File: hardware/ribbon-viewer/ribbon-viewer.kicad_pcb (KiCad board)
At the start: 2 copper layers, 96.5 x 73.7 mm, 186 parts, among them J1 Conn_01x40, J2 Conn_01x40, J3 Power, U1 74HC541, U2 74HC541, U3 74HC541, U4 74HC541, U5 74HC541, U6 MCP1825S

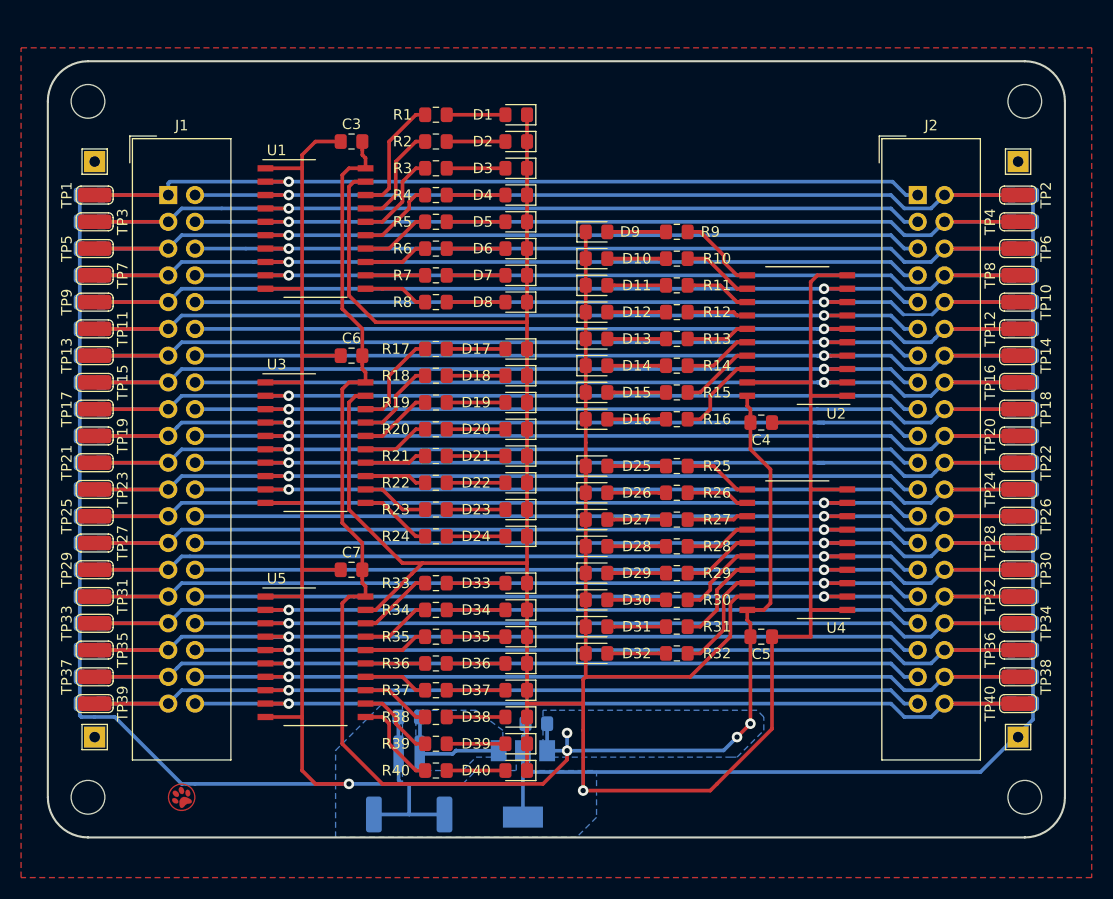
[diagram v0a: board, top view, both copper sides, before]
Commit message: Updated layout
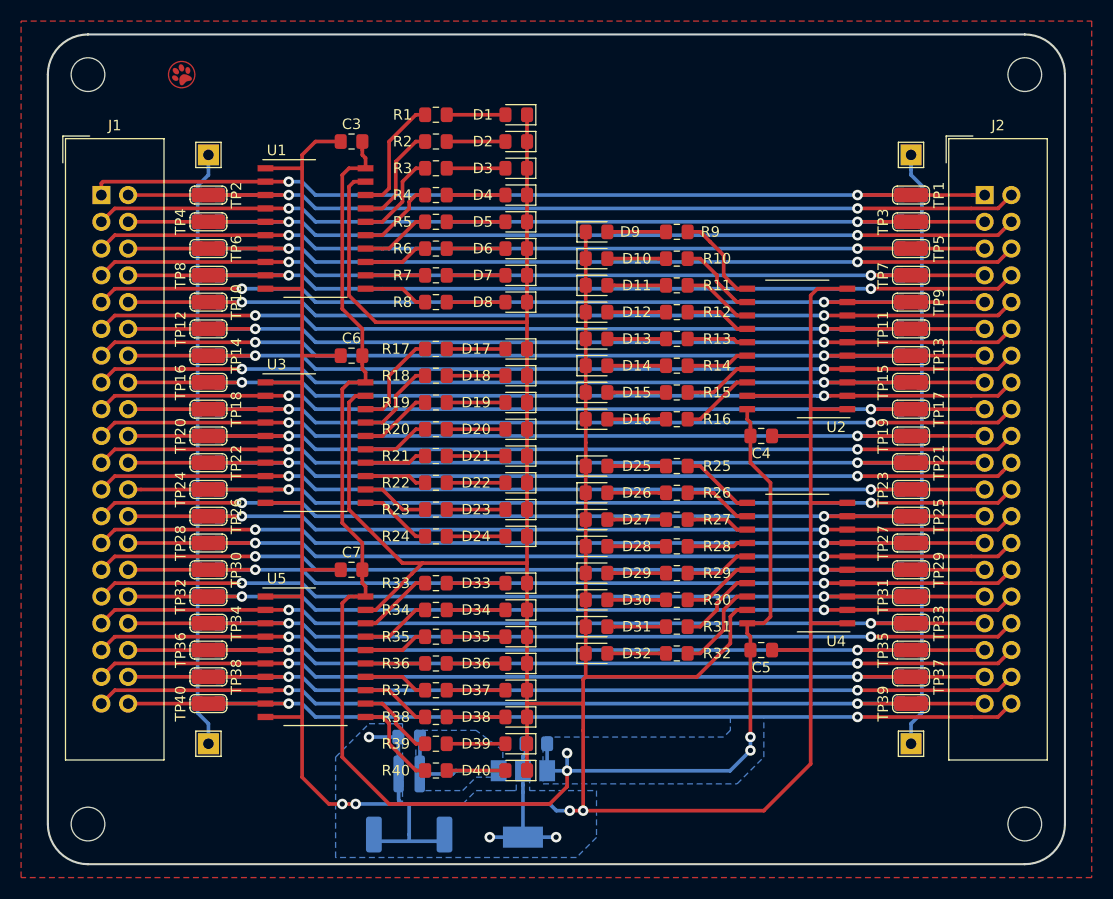
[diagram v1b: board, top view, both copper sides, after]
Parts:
- moved R41 77.9 mm to (134.0, 50.8), turned to 180 degrees
- moved R43 77.9 mm to (134.0, 53.3), turned to 180 degrees
- moved R45 77.9 mm to (134.0, 55.9), turned to 180 degrees
- moved R47 77.9 mm to (134.0, 58.4), turned to 180 degrees
- moved R49 77.9 mm to (134.0, 61.0), turned to 180 degrees
- moved R51 77.9 mm to (134.0, 63.5), turned to 180 degrees
- moved R53 77.9 mm to (134.0, 66.0), turned to 180 degrees
- moved R55 77.9 mm to (134.0, 68.6), turned to 180 degrees
- moved R57 77.9 mm to (134.0, 71.1), turned to 180 degrees
- moved R59 77.9 mm to (134.0, 73.7), turned to 180 degrees
- moved R61 77.9 mm to (134.0, 76.2), turned to 180 degrees
- moved R63 77.9 mm to (134.0, 78.7), turned to 180 degrees
- moved R65 77.9 mm to (134.0, 81.3), turned to 180 degrees
- moved R67 77.9 mm to (134.0, 83.8), turned to 180 degrees
- moved R69 77.9 mm to (134.0, 86.4), turned to 180 degrees
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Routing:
- net GND: track 617.6 -> 575.7 mm, vias 2 -> 7
- net /D38: track 87.7 -> 92.1 mm, vias 1 -> 2
- net /D29: track 87.7 -> 92.1 mm, vias 1 -> 2
- net /D27: track 87.7 -> 92.1 mm, vias 1 -> 2
- net /D25: track 87.7 -> 92.1 mm, vias 1 -> 2
- net /D15: track 87.7 -> 92.1 mm, vias 1 -> 2
- net /D9: track 87.7 -> 92.1 mm, vias 1 -> 2
- net /D31: track 87.7 -> 92.1 mm, vias 1 -> 2
- net /D11: track 87.7 -> 92.1 mm, vias 1 -> 2
- net /D8: track 87.7 -> 91.5 mm, vias 1 -> 2
- net /D6: track 87.7 -> 91.5 mm, vias 1 -> 2
- net /D40: track 87.7 -> 91.5 mm, vias 1 -> 2
- net /D4: track 87.7 -> 91.5 mm, vias 1 -> 2
- net /D36: track 87.7 -> 91.5 mm, vias 1 -> 2
- net /D34: track 87.7 -> 91.5 mm, vias 1 -> 2
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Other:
- board size 96.5 x 73.7 mm -> 96.5 x 78.7 mm

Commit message: Change testpoints to pin header
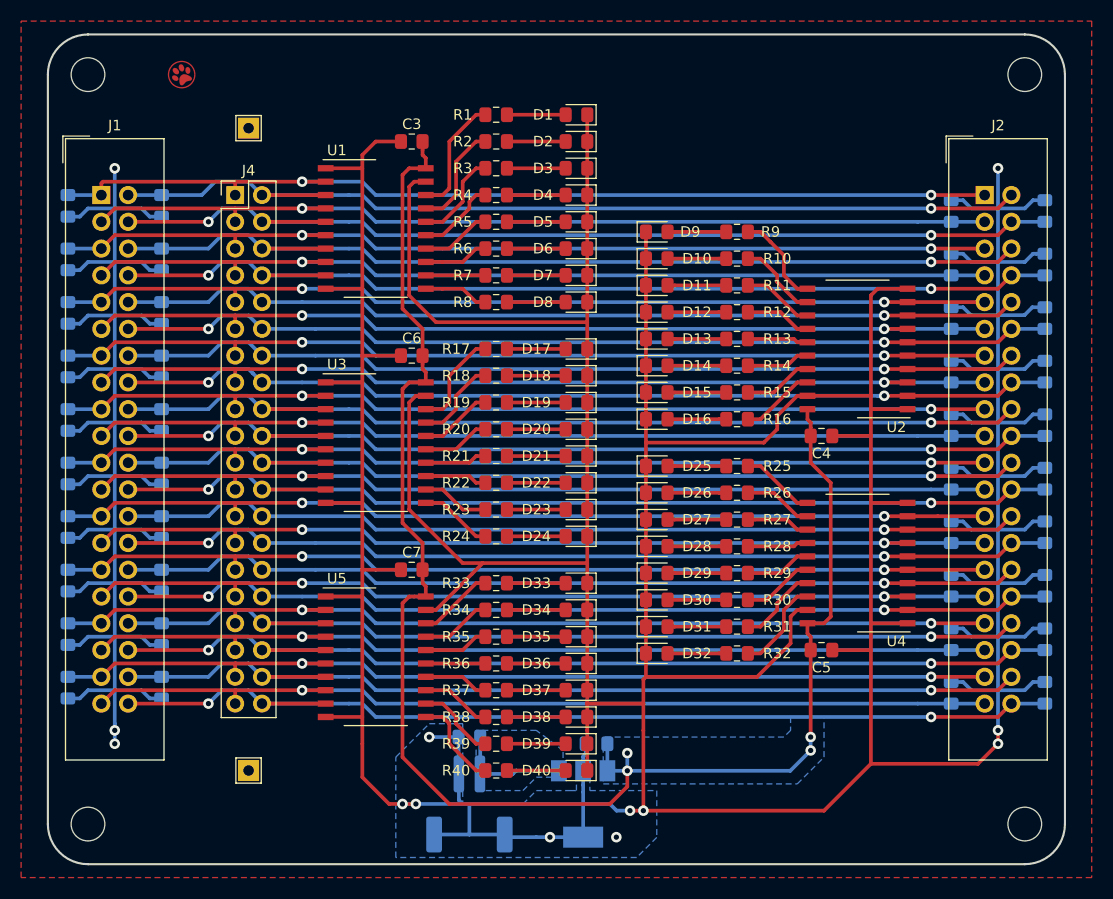
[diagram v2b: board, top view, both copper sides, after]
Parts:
- removed TP1, TP10, TP11, TP12, TP13, TP14, TP15, TP16, TP17, TP18, TP19, TP2, TP20, TP21, TP22, TP23, TP24, TP25, TP26, TP27, TP28, TP29, TP3, TP30, TP31, TP32, TP33, TP34, TP35, TP36, TP37, TP38, TP39, TP4, TP40, TP5, TP6, TP7, TP8, TP9: TestPoint, riscv-serial:TestPoint-0805
- removed TP43, TP44: TestPoint, TestPoint:TestPoint_THTPad_2.0x2.0mm_Drill1.0mm
- added J4: Conn_01x40, Connector_PinHeader_2.54mm:PinHeader_2x20_P2.54mm_Vertical, F.Cu at (69.8, 50.8)
- moved TP41 85.8 mm to (71.1, 105.4), turned to 180 degrees
- moved R41 80.0 mm to (54.0, 51.8), turned to 90 degrees
- moved R45 80.0 mm to (54.0, 56.9), turned to 90 degrees
- moved R49 80.0 mm to (54.0, 62.0), turned to 90 degrees
- moved R53 80.0 mm to (54.0, 67.1), turned to 90 degrees
- moved R57 80.0 mm to (54.0, 72.1), turned to 90 degrees
- moved R61 80.0 mm to (54.0, 77.2), turned to 90 degrees
- moved R65 80.0 mm to (54.0, 82.3), turned to 90 degrees
- moved R69 80.0 mm to (54.0, 87.4), turned to 90 degrees
- moved R73 80.0 mm to (54.0, 92.5), turned to 90 degrees
- moved R77 80.0 mm to (54.0, 97.5), turned to 90 degrees
- moved R44 79.4 mm to (146.7, 52.3), turned to 270 degrees
- moved R48 79.4 mm to (146.7, 57.4), turned to 270 degrees
- moved R52 79.4 mm to (146.7, 62.5), turned to 270 degrees
- moved R56 79.4 mm to (146.7, 67.6), turned to 270 degrees
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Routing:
- net GND: track 575.7 -> 792.3 mm, vias 7 -> 13
- net /D17: track 87.7 -> 91.6 mm
- net /D33: track 87.7 -> 91.6 mm
- net /D27: track 92.1 -> 88.4 mm
- net /D15: track 92.1 -> 88.4 mm
- net /D11: track 92.1 -> 88.4 mm
- net /D31: track 92.1 -> 88.4 mm
- net /D36: track 91.5 -> 95.1 mm
- net /D20: track 91.5 -> 95.1 mm
- net /D8: track 91.5 -> 95.1 mm
- net /D40: track 91.5 -> 95.1 mm
- net /D4: track 91.5 -> 95.1 mm
- net /D24: track 91.5 -> 95.1 mm
- net /D29: track 92.1 -> 89.3 mm
- net /D25: track 92.1 -> 89.3 mm
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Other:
- board text added: "2020-12-31"
- board text removed: "2020-12-29"

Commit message: Finished layout
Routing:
- net VCC: track 150.8 -> 142.7 mm, vias 4 -> 3
- net GND: track 792.3 -> 794.0 mm
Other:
- board text added: "JLCJLCJLCJLC"

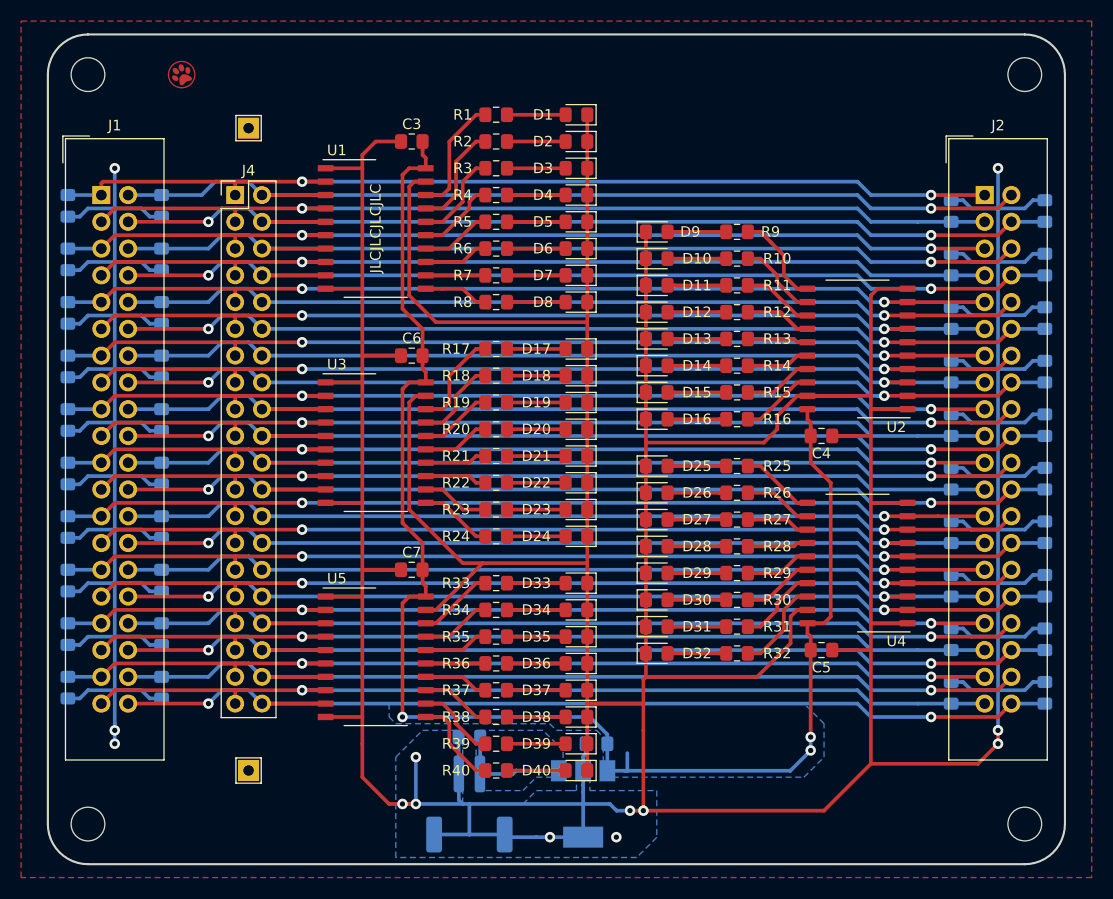
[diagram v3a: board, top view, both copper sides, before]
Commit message: Update all to Kicad 6
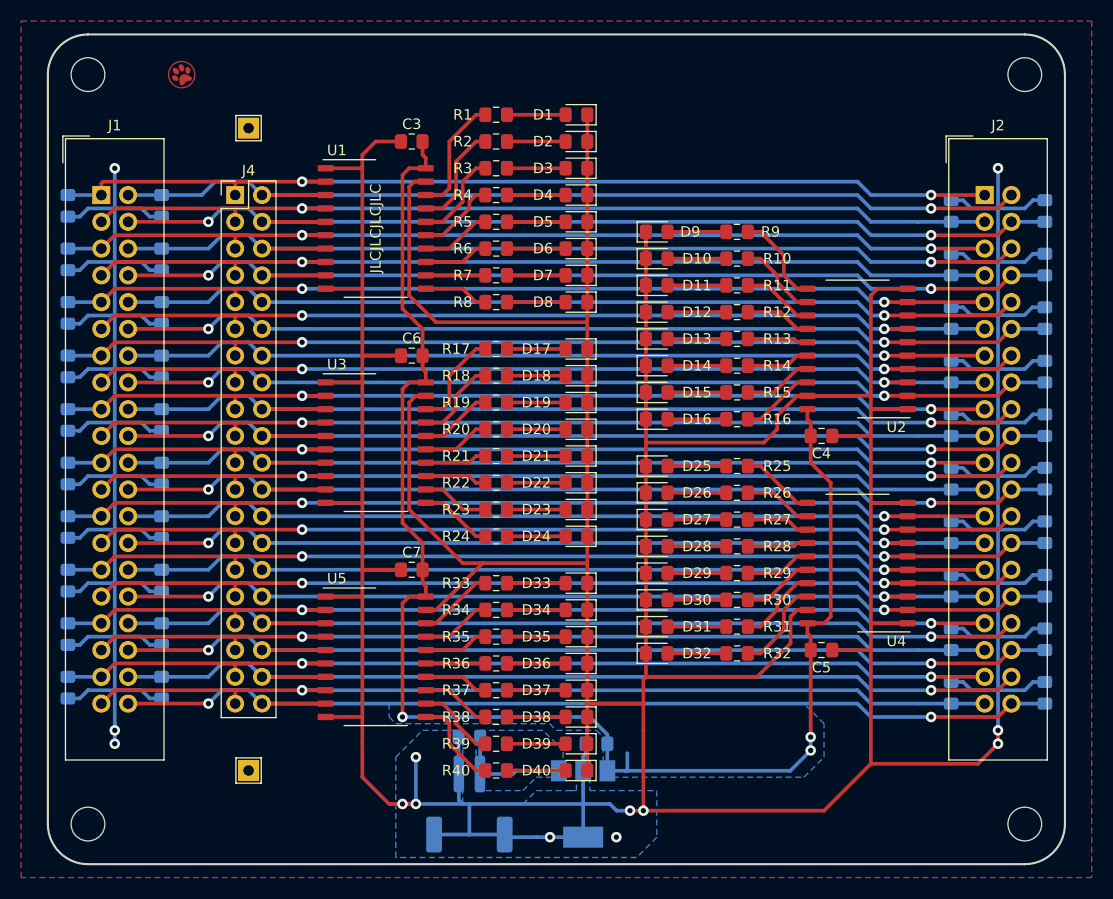
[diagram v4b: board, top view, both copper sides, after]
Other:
- net class Default removed
